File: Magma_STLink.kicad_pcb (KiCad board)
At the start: 2 copper layers, 51.3 x 20.8 mm, 44 parts, among them J1 Conn_01x03, J2 Conn_01x03, J3 Conn_01x02, J4 Conn_01x02, J5 USB_A, U1 LM1117-3.3, U2 STM32F103C8Tx, Y1 Crystal

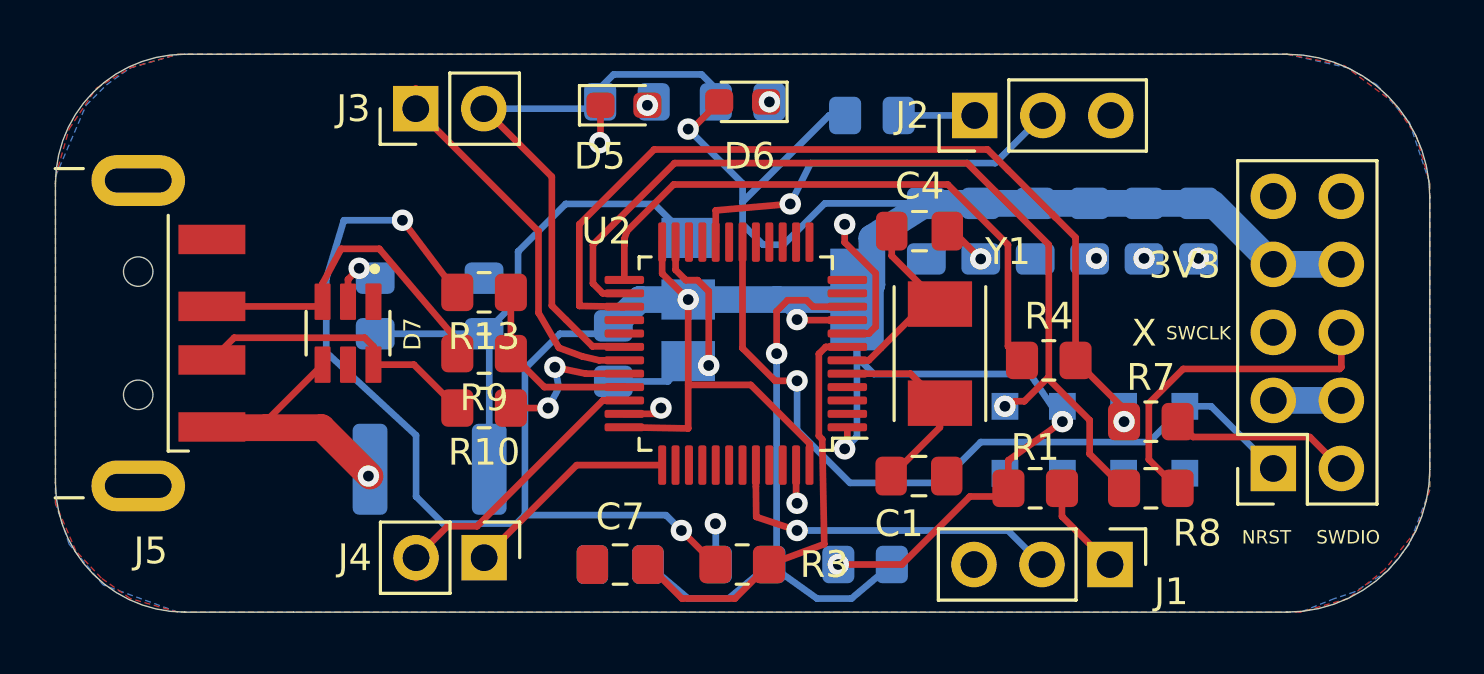
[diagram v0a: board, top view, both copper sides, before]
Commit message: Reset'e bir direnç eklendi. Anlık resetleyebilmek için 0805 kılıfında bir direnç eklendi.
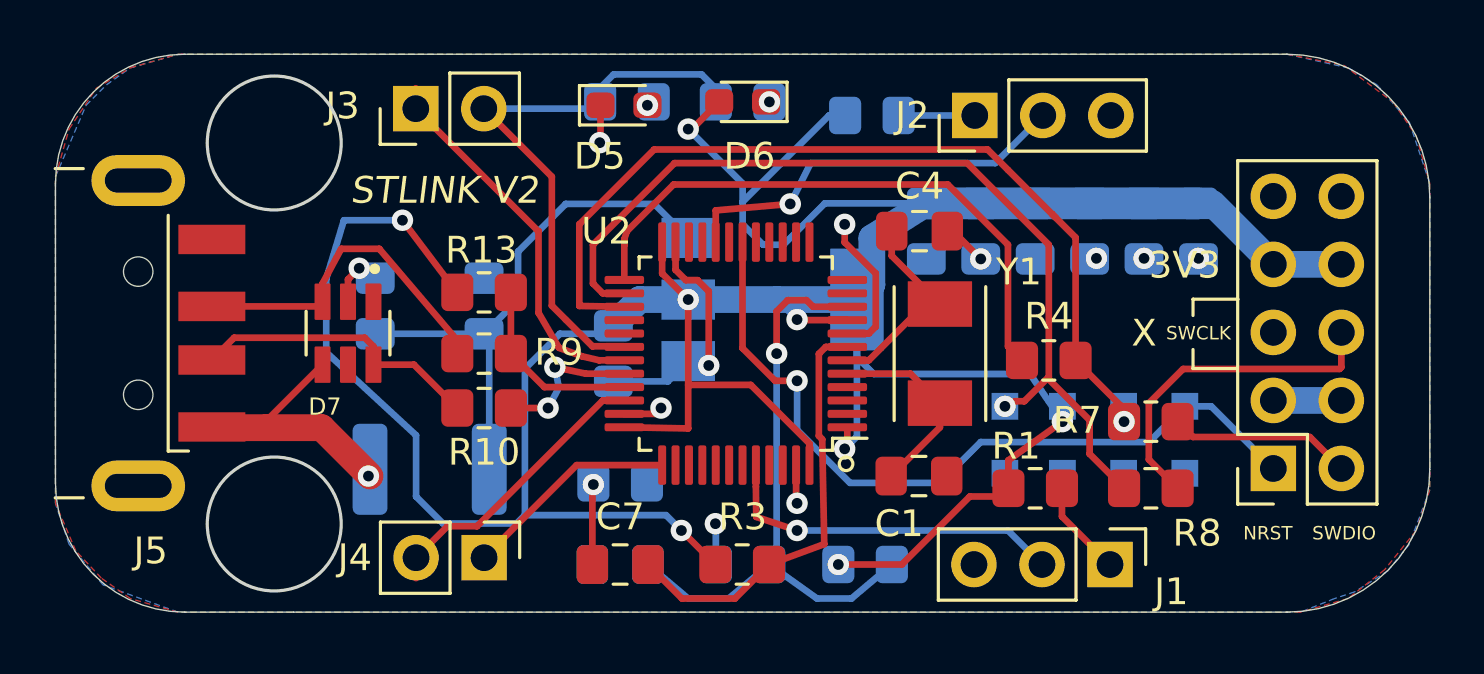
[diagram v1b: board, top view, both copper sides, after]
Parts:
- removed G***: LOGO, Logo:MagmaLogo_Kucuk
- added R14: 100K, Resistor_SMD:R_0805_2012Metric_Pad1.20x1.40mm_HandSolder, B.Cu at (55.4, 63.0)
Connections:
- C7 pad 2: GND -> Net-(C7-Pad2)
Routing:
- net Net-(C7-Pad2): track 0.00 -> 3.00 mm, vias 0 -> 1
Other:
- outline, holes or cut-outs redrawn
- board text added: "STLINK V2"

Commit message: Son Değişiklikler ve step
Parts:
- added G***: LOGO, Component Documents:MagmaLogoDahaKucuk, B.Cu at (63.0, 62.2)
- added G***: LOGO, Component Documents:STLogo, F.Cu at (73.4, 53.6)

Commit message: Update project to latest KiCAD version
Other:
- net class Default removed
- net class USB removed
